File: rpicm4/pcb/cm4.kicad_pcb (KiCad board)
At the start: 2 copper layers, 85.6 x 55 mm, 3 parts, among them J1 USB_C_Receptacle_USB2.0, J2 USB_C_Receptacle_USB2.0

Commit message: rpicm4 usb
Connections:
- J2 pad B6: Net-(J2-PadB6) -> /USB_P
- J2 pad B7: Net-(J2-PadB7) -> /USB_N
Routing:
- net +5V: track 114.5 -> 134.3 mm
- net /USB_P: track 24.8 -> 40.0 mm
- net /USB_N: track 25.2 -> 38.7 mm
- net GND: track 144.7 -> 135.4 mm

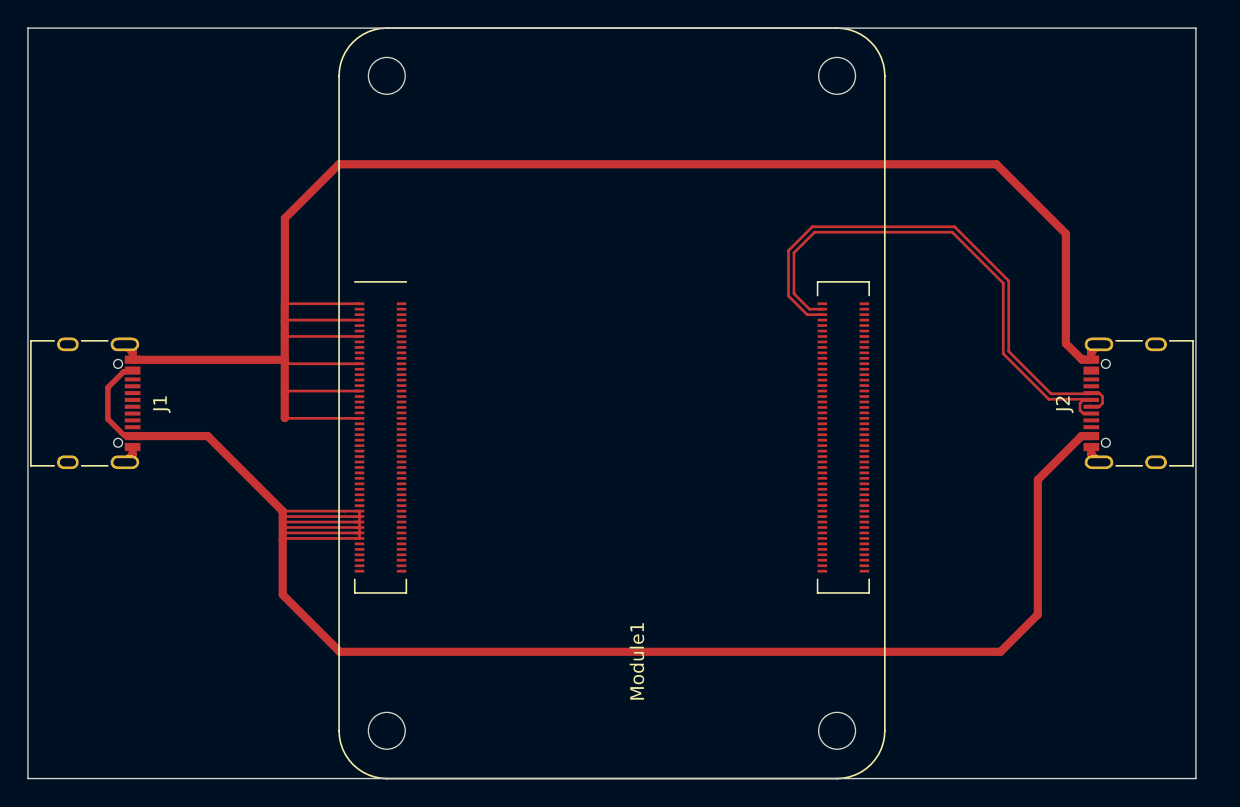
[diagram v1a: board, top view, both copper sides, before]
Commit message: rpicm4: typec ufp/dfp
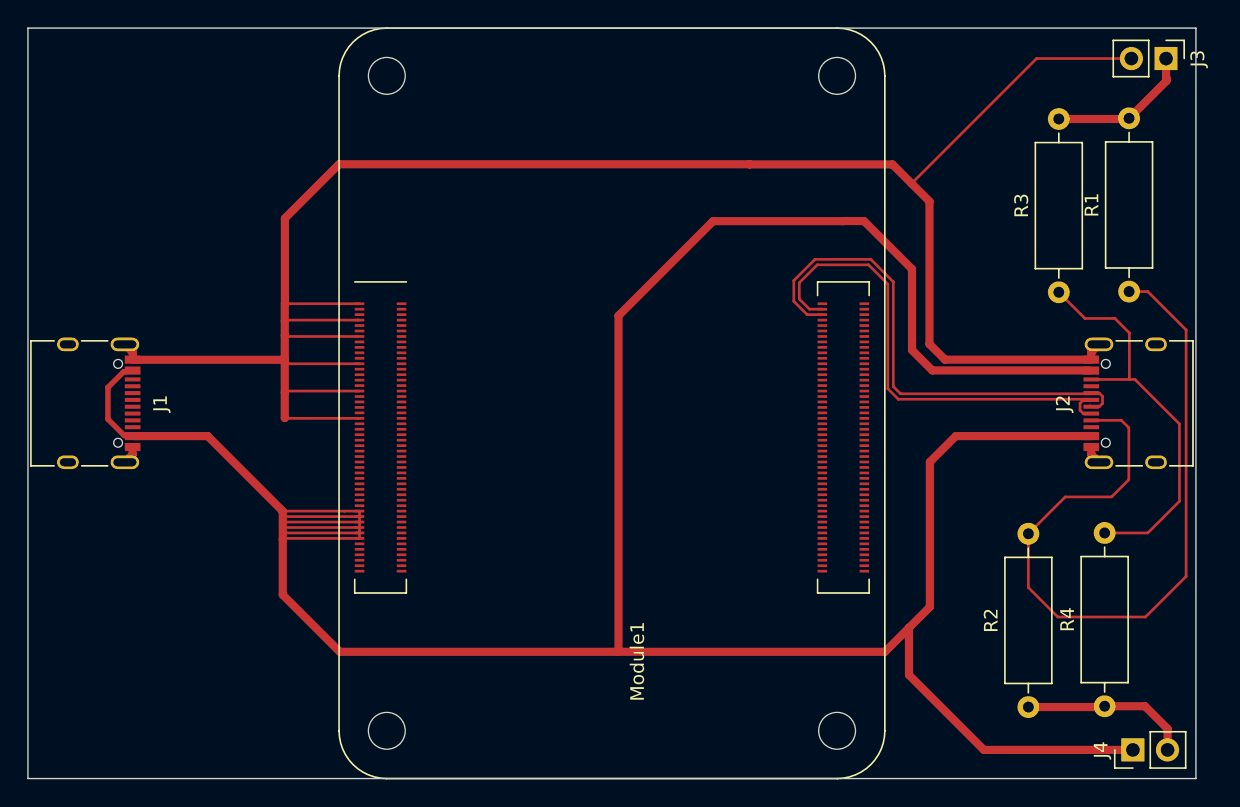
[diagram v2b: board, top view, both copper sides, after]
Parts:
- added J3: Conn_01x02_Male, Connector_PinHeader_2.54mm:PinHeader_1x02_P2.54mm_Vertical, F.Cu at (140.6, 47.2)
- added J4: Conn_01x02_Male, Connector_PinHeader_2.54mm:PinHeader_1x02_P2.54mm_Vertical, F.Cu at (138.2, 97.9)
- added R1: R, Resistor_THT:R_Axial_DIN0309_L9.0mm_D3.2mm_P12.70mm_Horizontal, F.Cu at (137.9, 64.3)
- added R2: R, Resistor_THT:R_Axial_DIN0309_L9.0mm_D3.2mm_P12.70mm_Horizontal, F.Cu at (130.5, 94.8)
- added R3: R, Resistor_THT:R_Axial_DIN0309_L9.0mm_D3.2mm_P12.70mm_Horizontal, F.Cu at (132.8, 64.4)
- added R4: R, Resistor_THT:R_Axial_DIN0309_L9.0mm_D3.2mm_P12.70mm_Horizontal, F.Cu at (136.1, 94.7)
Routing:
- net +5V: track 134.3 -> 227.0 mm
- net Net-(J2-PadA5): track 0.00 -> 56.8 mm
- net Net-(J2-PadB5): track 0.00 -> 29.7 mm
- net GND: track 135.4 -> 156.8 mm
- net Net-(J4-Pad2): track 0.00 -> 12.5 mm
- net Net-(J3-Pad1): track 0.00 -> 10.7 mm
- net /USB_P: track 40.0 -> 37.6 mm
- net /USB_N: track 38.7 -> 36.3 mm

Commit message: rpicm4: dwc2 host/device
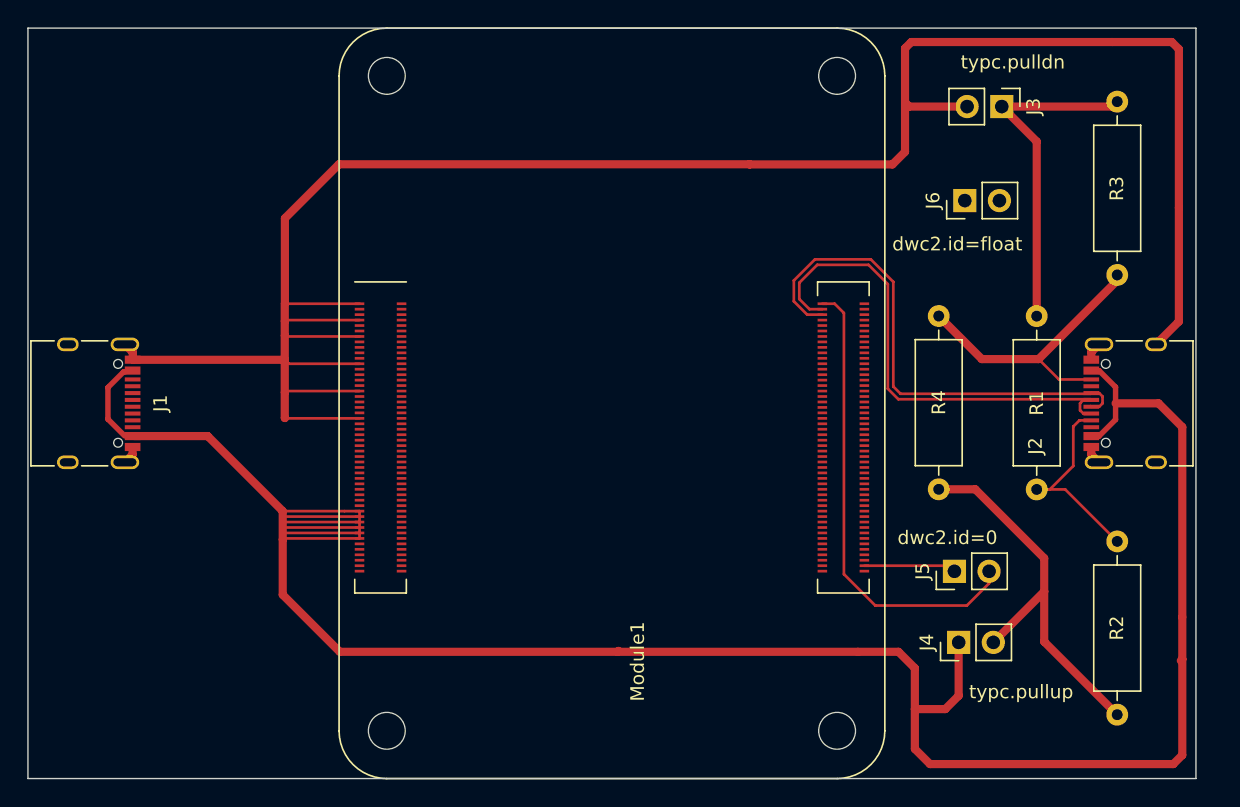
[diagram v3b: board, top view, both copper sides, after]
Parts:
- added J5: Conn_01x02_Male, Connector_PinHeader_2.54mm:PinHeader_1x02_P2.54mm_Vertical, F.Cu at (125.1, 84.8)
- added J6: Conn_01x02_Male, Connector_PinHeader_2.54mm:PinHeader_1x02_P2.54mm_Vertical, F.Cu at (125.9, 57.6)
- R1, R3: value R -> 5.1k
- R2, R4: value R -> 22k
- moved R4 20.0 mm to (124.0, 78.8)
- moved R1 16.0 mm to (131.1, 78.8)
- moved J4 15.0 mm to (125.4, 90.0)
- moved J3 12.5 mm to (128.6, 50.8)
- moved R2 6.53 mm to (137.0, 95.3)
- moved R3 4.46 mm to (137.0, 63.1)
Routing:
- net +5V: track 227.0 -> 179.3 mm
- net Net-(J2-PadA5): track 56.8 -> 15.3 mm
- net Net-(Module1-Pad101): track 0.00 -> 34.1 mm
- net GND: track 156.8 -> 173.4 mm
- net Net-(J4-Pad2): track 12.5 -> 28.8 mm
- net Net-(J3-Pad1): track 10.7 -> 25.0 mm
- net Net-(J2-PadB5): track 29.7 -> 21.7 mm
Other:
- board text added: "dwc2.id=0"
- board text added: "dwc2.id=float"
- board text added: "typc.pulldn"
- board text added: "typc.pullup"

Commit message: rpicm4: usb mode
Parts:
- R1, R2, R3, R4: footprint Resistor_THT:R_Axial_DIN0309_L9.0mm_D3.2mm_P12.70mm_Horizontal -> Resistor_THT:R_Axial_DIN0207_L6.3mm_D2.5mm_P10.16mm_Horizontal
- moved J4 14.6 mm to (138.8, 96.0), turned to -90 degrees
- moved R2 11.9 mm to (127.8, 87.7)
- moved J5 11.5 mm to (128.4, 95.9), turned to -90 degrees
- moved R3 10.2 mm to (127.8, 67.5)
- moved J6 8.78 mm to (125.5, 48.9)
- moved J3 7.62 mm to (135.9, 48.9), turned to 90 degrees
- moved R1 1.36 mm to (131.6, 77.5)
- moved R4 1.18 mm to (124.0, 77.6)
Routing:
- net Net-(J2-PadB5): track 21.7 -> 12.5 mm
- net +5V: track 179.3 -> 173.1 mm
- net GND: track 173.4 -> 178.9 mm
- net Net-(J2-PadA5): track 15.3 -> 9.78 mm
- net Net-(J4-Pad2): track 28.8 -> 25.4 mm
- net Net-(J5-Pad2): track 34.1 -> 35.5 mm
- net Net-(J3-Pad1): track 25.0 -> 26.1 mm
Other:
- board text added: "<gadg mode>"
- board text added: "<host mode>"

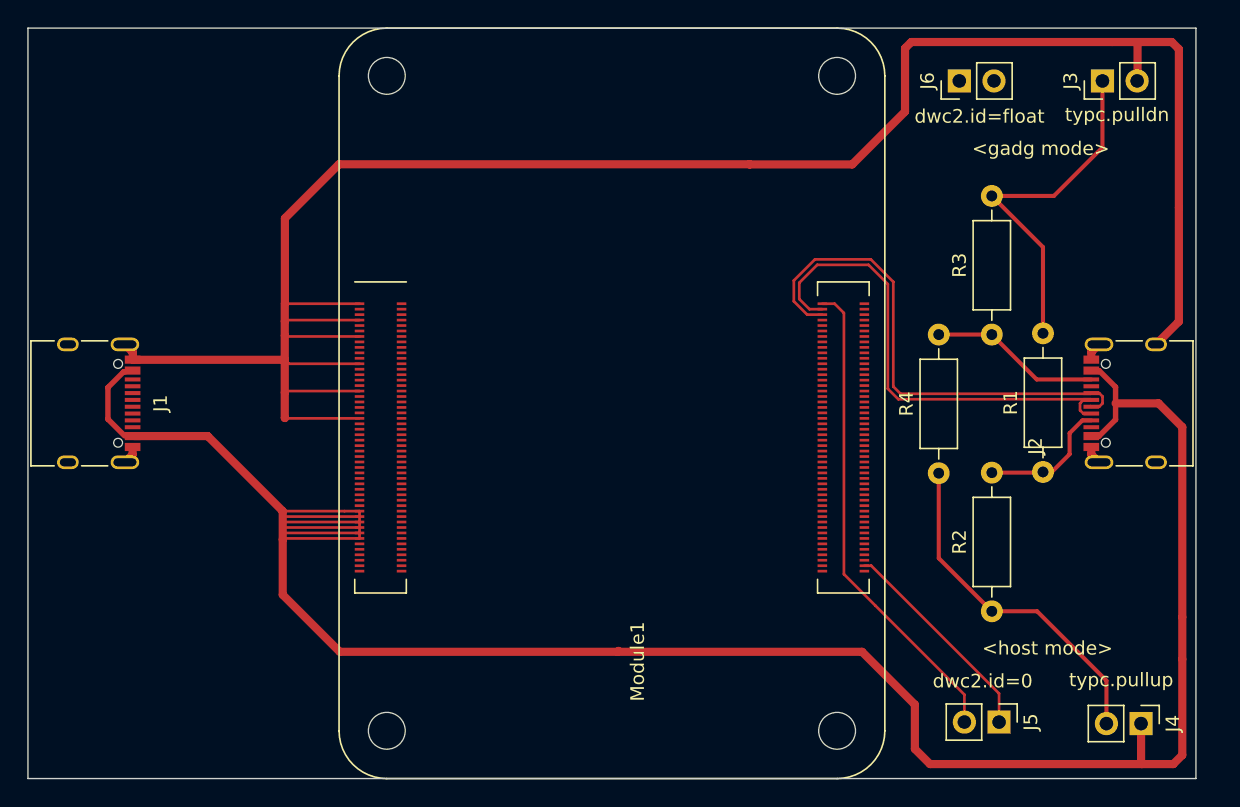
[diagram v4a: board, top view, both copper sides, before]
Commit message: rpicm4: nRPIBOOT, UART, typec.cc
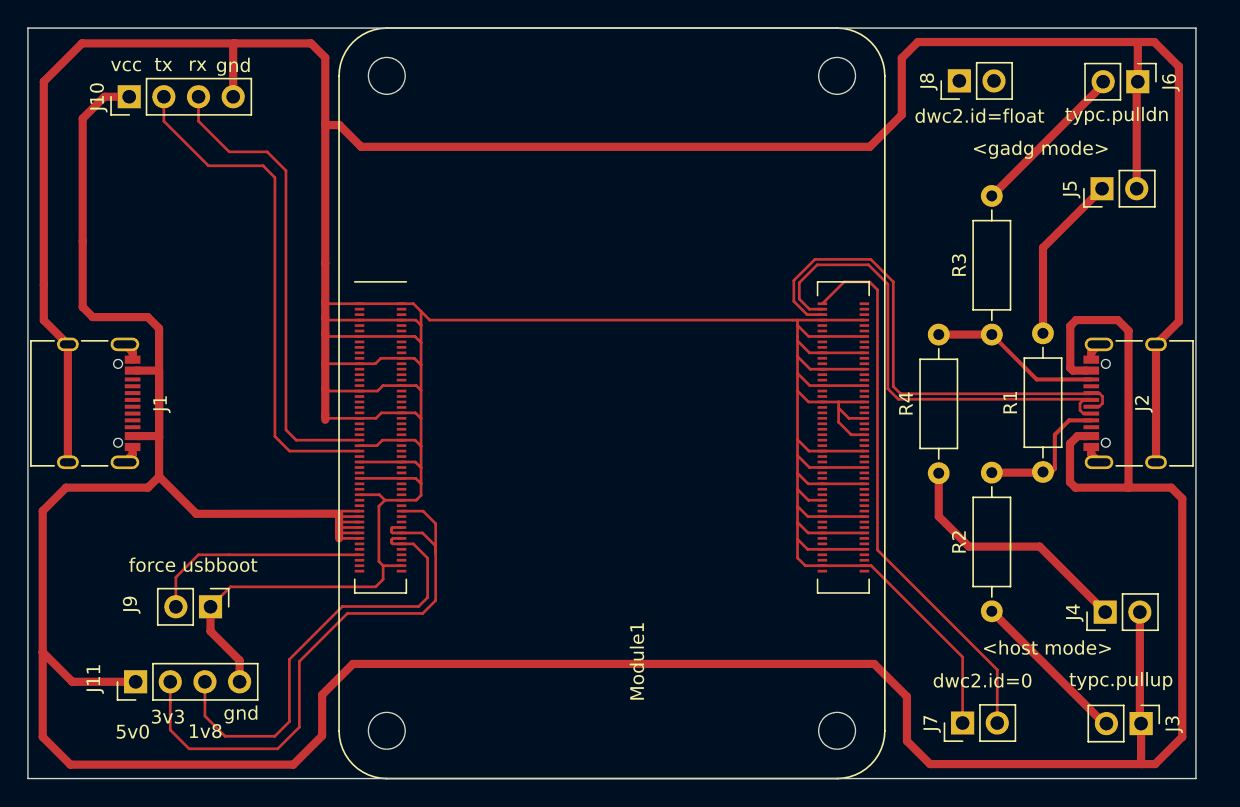
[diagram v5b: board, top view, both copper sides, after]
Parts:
- added J10: Conn_01x04_Male, Connector_PinHeader_2.54mm:PinHeader_1x04_P2.54mm_Vertical, F.Cu at (64.6, 50.0)
- added J11: Conn_01x04_Male, Connector_PinHeader_2.54mm:PinHeader_1x04_P2.54mm_Vertical, F.Cu at (65.1, 92.9)
- added J4: Conn_01x02_Male, Connector_PinHeader_2.54mm:PinHeader_1x02_P2.54mm_Vertical, F.Cu at (136.2, 87.8)
- added J6: Conn_01x02_Male, Connector_PinHeader_2.54mm:PinHeader_1x02_P2.54mm_Vertical, F.Cu at (138.5, 48.9)
- added J9: Conn_01x02_Male, Connector_PinHeader_2.54mm:PinHeader_1x02_P2.54mm_Vertical, F.Cu at (70.6, 87.4)
- moved J5 7.90 mm to (135.9, 56.8)
- moved J7 2.67 mm to (125.7, 95.9), turned to 90 degrees
- renumbered J4 to J3, J3 to J5, J5 to J7, J6 to J8
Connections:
- J3 pad 2: Net-(J4-Pad2) -> Net-(J3-Pad2)
- J5 pad 1: Net-(J3-Pad1) -> Net-(J5-Pad1)
- Module1 pad 78: Net-(Module1-Pad78) -> Net-(J11-Pad2)
- Module1 pad 84: Net-(Module1-Pad84) -> Net-(J11-Pad2)
- Module1 pad 86: Net-(Module1-Pad86) -> Net-(J11-Pad2)
- Module1 pad 90: Net-(Module1-Pad90) -> Net-(Module1-Pad88)
- R1 pad 2: Net-(J3-Pad1) -> Net-(J5-Pad1)
- R2 pad 1: Net-(J4-Pad2) -> Net-(J3-Pad2)
- R3 pad 2: Net-(J3-Pad1) -> Net-(J6-Pad2)
- R4 pad 1: Net-(J4-Pad2) -> Net-(J4-Pad1)
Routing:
- net GND: track 178.9 -> 436.7 mm
- net +5V: track 173.1 -> 259.7 mm
- net Net-(J11-Pad2): track 0.00 -> 44.7 mm
- net Net-(Module1-Pad55): track 0.00 -> 37.3 mm
- net Net-(Module1-Pad51): track 0.00 -> 34.4 mm
- net Net-(Module1-Pad88): track 0.00 -> 33.3 mm
- net Net-(J3-Pad1): track 26.1 -> 0.00 mm
- net Net-(J4-Pad2): track 25.4 -> 0.00 mm
- net Net-(J4-Pad1): track 0.00 -> 18.3 mm
- net Net-(Module1-Pad93): track 0.00 -> 16.3 mm
- net Net-(J5-Pad1): track 0.00 -> 12.4 mm
- net Net-(J6-Pad2): track 0.00 -> 11.7 mm
- net Net-(J3-Pad2): track 0.00 -> 11.2 mm
- net Net-(J7-Pad2): track 35.5 -> 40.3 mm
- net Net-(J2-PadA5): track 9.78 -> 10.3 mm
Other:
- board text added: "1v8"
- board text added: "3v3"
- board text added: "5v0"
- board text added: "force usbboot"
- board text added: "gnd"
- board text added: "rx"
- board text added: "tx"
- board text added: "vcc"

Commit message: rpicm4: led pwr/act,analog 0/1,pwm 0/1,uart tx/rx
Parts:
- added J12: Conn_01x04_Male, Connector_PinHeader_2.54mm:PinHeader_1x04_P2.54mm_Vertical, F.Cu at (66.2, 58.2)
- added J16: Conn_01x04_Male, Connector_PinHeader_2.54mm:PinHeader_1x04_P2.54mm_Vertical, F.Cu at (71.9, 93.3)
- J10: value Conn_01x04_Male -> Conn_01x02_Male; footprint Connector_PinHeader_2.54mm:PinHeader_1x04_P2.54mm_Vertical -> Connector_PinHeader_2.54mm:PinHeader_1x02_P2.54mm_Vertical
- moved J11 43.5 mm to (72.0, 50.0), turned to -90 degrees
- moved J10 34.8 mm to (72.0, 84.0), turned to 0 degrees
- moved J9 5.71 mm to (66.0, 84.0), turned to 0 degrees
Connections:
- net Net-(J2-PadA5) renamed /cc1
- net Net-(J2-PadB5) renamed /cc2
- J10 pad 1: +5V -> /eGLOBAL
- J10 pad 2: Net-(Module1-Pad55) -> GND
- J11 pad 1: +5V -> GND
- J11 pad 2: Net-(J11-Pad2) -> /1v8
- J11 pad 3: Net-(Module1-Pad88) -> /3v3
- J11 pad 4: GND -> +5V
- J9 pad 1: GND -> /nRPIBOOT
- J9 pad 2: Net-(Module1-Pad93) -> GND
- Module1 pad 174: Net-(Module1-Pad174) -> GND
- Module1 pad 21: Net-(Module1-Pad21) -> /actled
- Module1 pad 28: Net-(Module1-Pad28) -> /pwm1
- Module1 pad 31: Net-(Module1-Pad31) -> /pwm0
- Module1 pad 51: Net-(Module1-Pad51) -> /rx
- Module1 pad 55: Net-(Module1-Pad55) -> /tx
- Module1 pad 78: Net-(J11-Pad2) -> /3v3
- Module1 pad 84: Net-(J11-Pad2) -> /3v3
- Module1 pad 86: Net-(J11-Pad2) -> /3v3
- Module1 pad 88: Net-(Module1-Pad88) -> /1v8
- Module1 pad 90: Net-(Module1-Pad88) -> /1v8
- Module1 pad 93: Net-(Module1-Pad93) -> /nRPIBOOT
- Module1 pad 94: Net-(Module1-Pad94) -> /ana0
- Module1 pad 95: Net-(Module1-Pad95) -> /pwrled
- Module1 pad 96: Net-(Module1-Pad96) -> /ana1
- Module1 pad 99: Net-(Module1-Pad99) -> /eGLOBAL
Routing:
- net /actled: track 0.00 -> 81.4 mm
- net GND: track 436.7 -> 377.2 mm, vias 0 -> 2
- net /3v3: track 0.00 -> 53.5 mm
- net /1v8: track 0.00 -> 52.0 mm
- net Net-(J11-Pad2): track 44.7 -> 0.00 mm
- net Net-(Module1-Pad55): track 37.3 -> 0.00 mm
- net Net-(Module1-Pad51): track 34.4 -> 0.00 mm
- net Net-(Module1-Pad88): track 33.3 -> 0.00 mm
- net /tx: track 0.00 -> 29.6 mm
- net /rx: track 0.00 -> 26.9 mm
- net /ana1: track 0.00 -> 24.4 mm
- net /ana0: track 0.00 -> 23.4 mm
- net /pwm1: track 0.00 -> 23.1 mm
- net /pwrled: track 0.00 -> 22.1 mm
- net +5V: track 259.7 -> 238.5 mm, vias 0 -> 5
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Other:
- board text added: "0v0"
- board text added: "GlobalEn"
- board text added: "nRPIBOOT"
- board text added: "pwm0"
- board text added: "pwm1"
- board text removed: "force usbboot"
- board text removed: "gnd"
- board text removed: "vcc"
